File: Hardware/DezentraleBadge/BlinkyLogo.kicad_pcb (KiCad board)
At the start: 2 copper layers, 69.7 x 54.4 mm, 49 parts, among them SW101 Button, U101 CH32V003AxMx

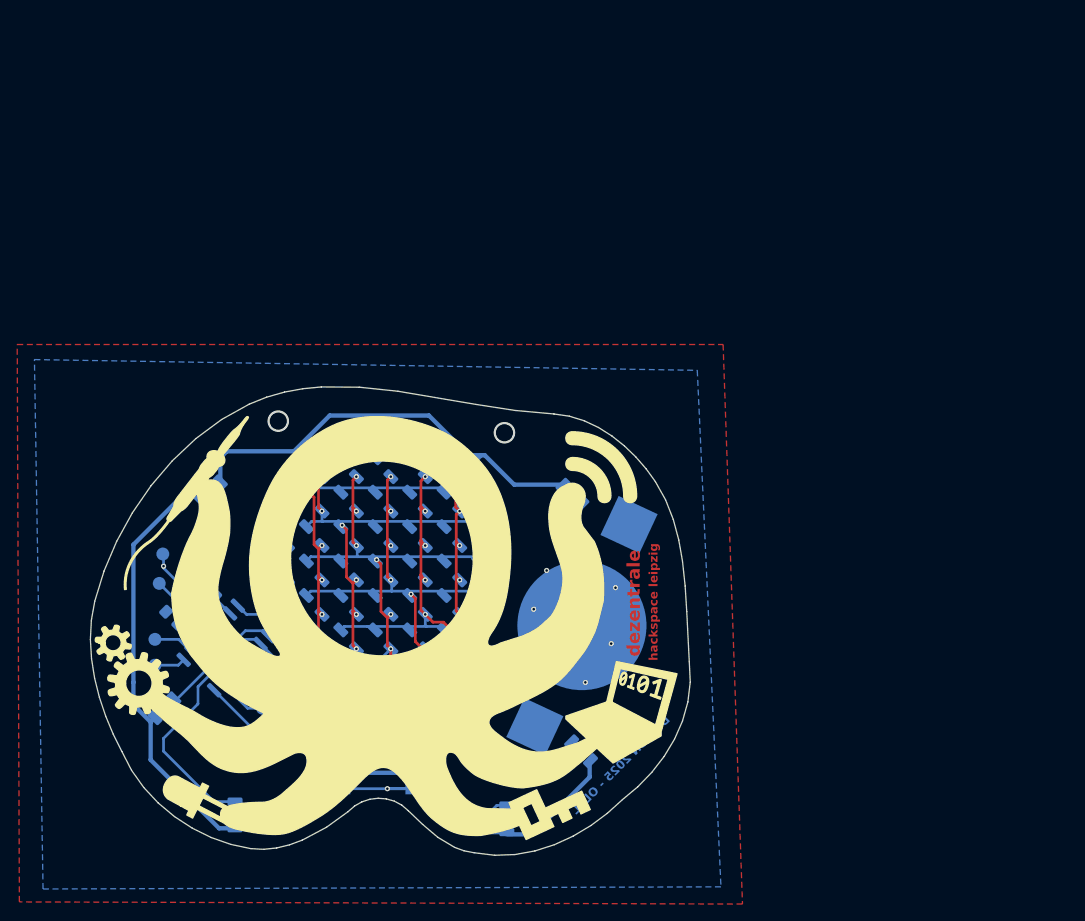
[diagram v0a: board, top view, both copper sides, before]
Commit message: Added schematic/pcb pdf files
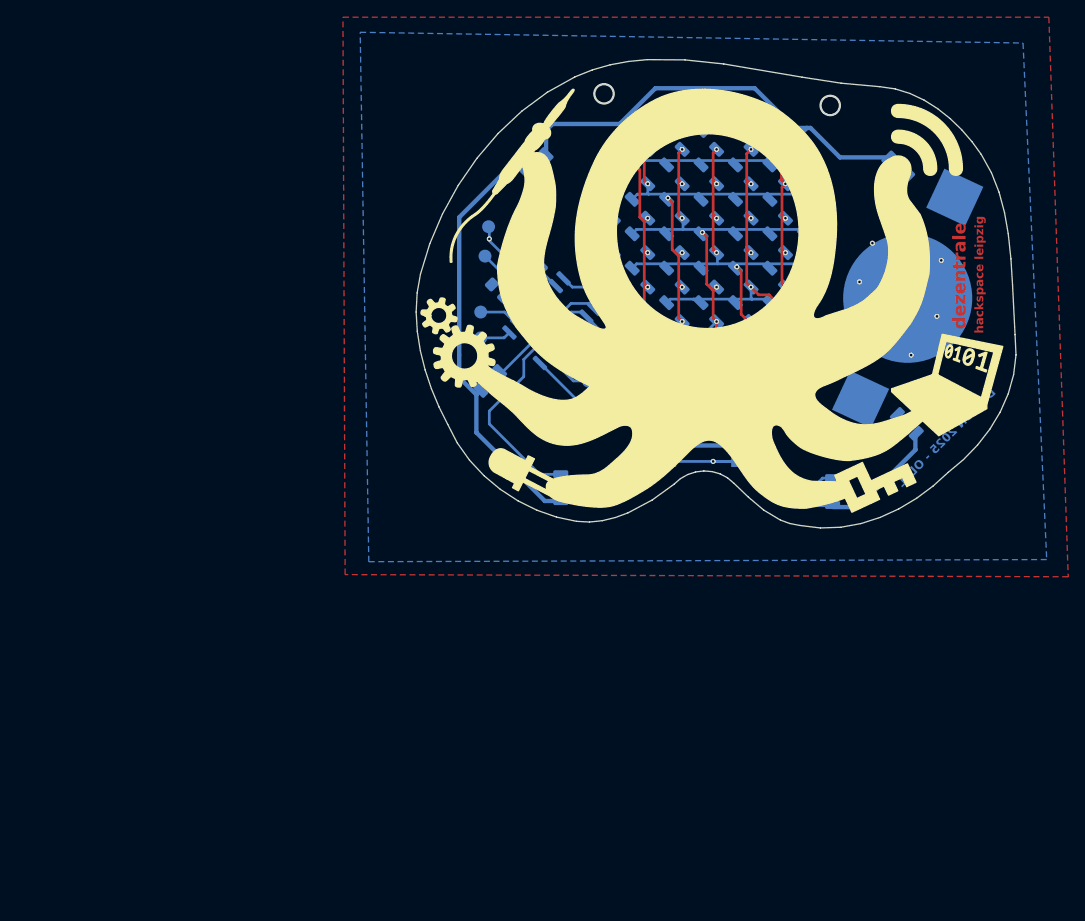
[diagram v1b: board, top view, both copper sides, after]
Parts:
- moved BT101 53.6 mm to (123.9, 63.4)
- moved C101 53.6 mm to (80.6, 60.5)
- moved D102 53.6 mm to (94.8, 45.0)
- moved D103 53.6 mm to (98.8, 45.0)
- moved D104 53.6 mm to (102.8, 45.0)
- moved D105 53.6 mm to (106.8, 45.0)
- moved D107 53.6 mm to (90.8, 49.0)
- moved D108 53.6 mm to (94.8, 49.0)
- moved D109 53.6 mm to (98.8, 49.0)
- moved D110 53.6 mm to (102.8, 49.0)
- moved D111 53.6 mm to (106.8, 49.0)
- moved D112 53.6 mm to (110.8, 49.0)
- moved D113 53.6 mm to (90.8, 53.0)
- moved D114 53.6 mm to (94.8, 53.0)
- moved D115 53.6 mm to (98.8, 53.0)
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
